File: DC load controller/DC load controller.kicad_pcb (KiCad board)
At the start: 2 copper layers, 54 x 25.4 mm, 29 parts, among them J1 Ctrl In, J2 Batt in, J3 Ctrl Out, J4 Pwr in, M1 3mm, M2 3mm, M3 3mm, Q1 BC547, Q2 BC557, U1 LM324

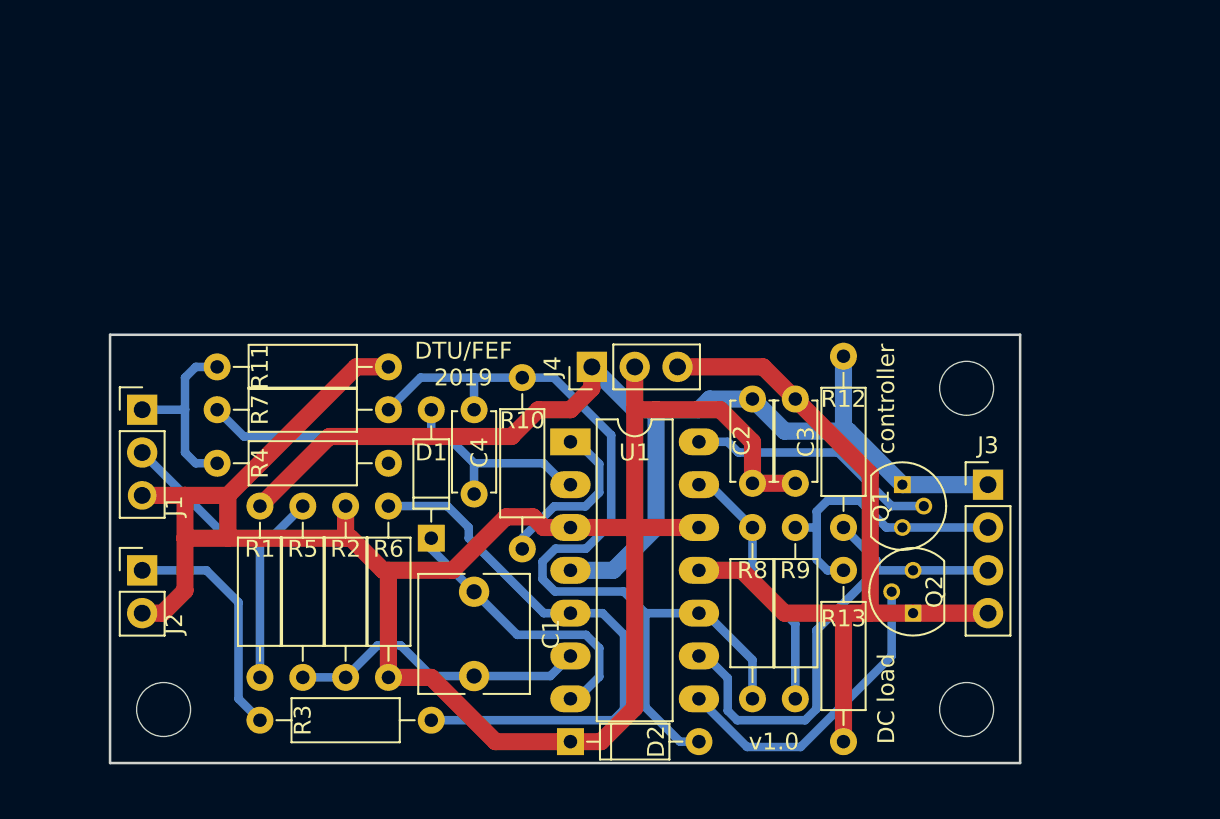
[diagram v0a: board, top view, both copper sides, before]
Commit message: Added extra output socket Layout changes
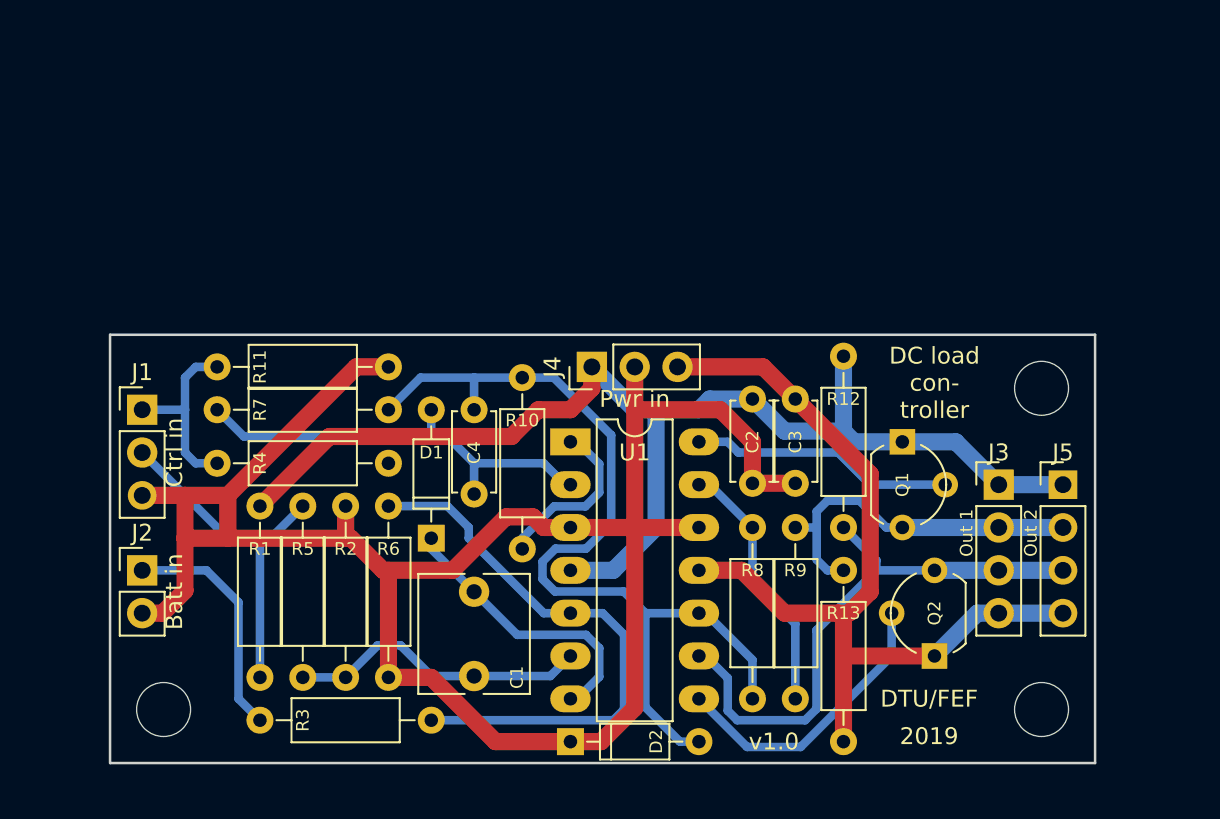
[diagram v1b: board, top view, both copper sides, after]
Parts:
- added J5: Ctrl Out 2, Pin_Headers:Pin_Header_Straight_1x04_Pitch2.54mm, F.Cu at (158.1, 72.4)
- J3: value Ctrl Out -> Ctrl Out 1
- Q1, Q2: footprint TO_SOT_Packages_THT:TO-92_Molded_Narrow -> TO_SOT_Packages_THT:TO-92_Molded_Wide
- moved M2 4.44 mm to (156.8, 85.7)
- moved M3 4.44 mm to (156.8, 66.7)
- moved Q2 2.84 mm to (150.5, 82.5)
- moved Q1 2.54 mm to (148.6, 69.8)
- moved J3 0.64 mm to (154.3, 72.4)
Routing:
- net VSS: track 48.3 -> 54.6 mm
- net Net-(J3-Pad3): track 30.0 -> 34.5 mm
- net VDD: track 68.3 -> 72.8 mm
- net Net-(J3-Pad2): track 17.1 -> 21.5 mm
- net Net-(Q2-Pad2): track 19.1 -> 17.8 mm
- net Net-(Q1-Pad2): track 15.4 -> 16.2 mm
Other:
- board size 54 x 25.4 mm -> 58.4 x 25.4 mm
- board text added: "Batt in"
- board text added: "Ctrl in"
- board text added: "DC load con- troller"
- board text added: "Out 1"
- board text added: "Out 2"
- board text added: "Pwr in"
- board text removed: "DC load"
- board text removed: "controller"

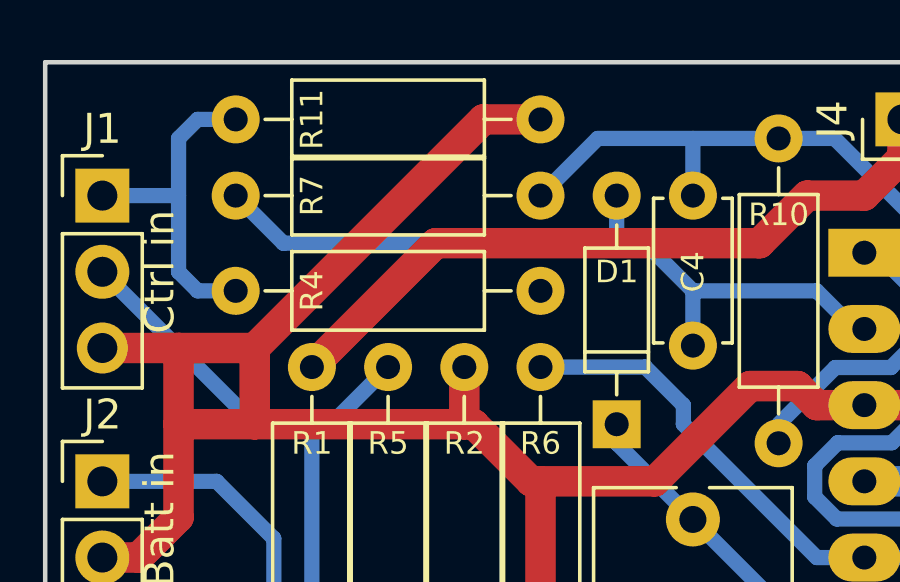
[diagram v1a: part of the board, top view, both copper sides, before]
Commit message: Fix wrong wire in schematics and pcb
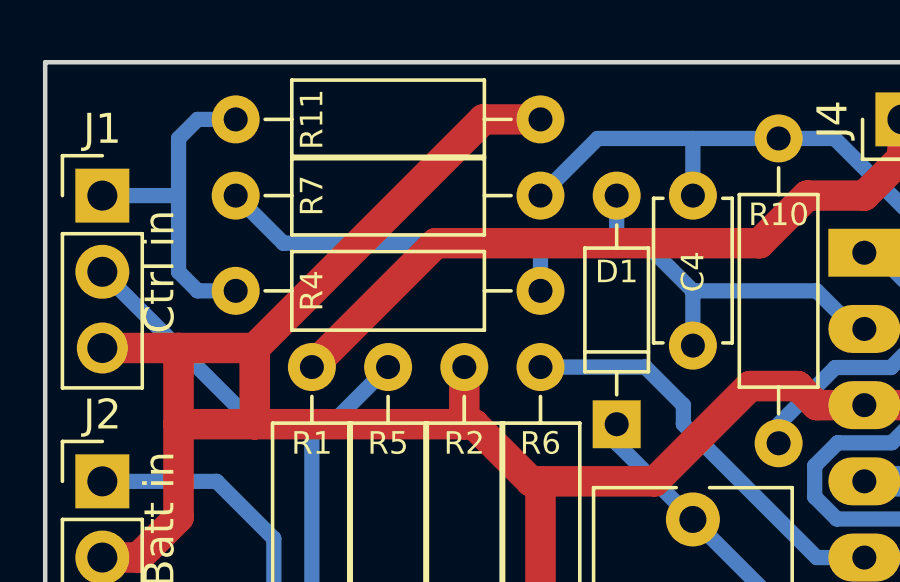
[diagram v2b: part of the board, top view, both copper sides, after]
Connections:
- R4 pad 1: Net-(R4-Pad1) -> Net-(C4-Pad1)
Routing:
- net Net-(C4-Pad1): track 26.6 -> 28.2 mm
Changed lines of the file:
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@@
 (kicad_pcb (version 4) (host pcbnew 4.0.6)
   (general
-    (links 56)
-    (no_connects 4)
-    (area 101.524999 63.424999 158.190001 88.975001)
+    (links 57)
+    (no_connects 1)
+    (area 101.524999 63.424999 160.095001 88.975001)
     (thickness 1.6)
     (drawings 13)
-    (tracks 199)
+    (tracks 201)
     (zones 0)
     (modules 30)
-    (nets 19)
+    (nets 18)
   )
   (page User 210.007 148.006)
@@
   )
   (setup
-    (last_trace_width 1.016)
+    (last_trace_width 0.508)
     (user_trace_width 0.254)
     (user_trace_width 0.508)
@@
   (net 16 "Net-(Q1-Pad2)")
   (net 17 "Net-(Q2-Pad2)")
-  (net 18 "Net-(R4-Pad1)")
   (net_class Default "This is the default net class."
     (clearance 0.2)
@@
     (add_net "Net-(R10-Pad2)")
     (add_net "Net-(R3-Pad1)")
-    (add_net "Net-(R4-Pad1)")
     (add_net "Net-(R8-Pad1)")
     (add_net VDD)
@@
     (fp_line (start 11.25 -1.6) (end -1.05 -1.6) (layer F.CrtYd) (width 0.05))
     (pad 1 thru_hole circle (at 0 0 180) (size 1.6 1.6) (drill 0.8) (layers *.Cu *.Mask)
-      (net 18 "Net-(R4-Pad1)"))
+      (net 13 "Net-(C4-Pad1)"))
     (pad 2 thru_hole oval (at 10.16 0 180) (size 1.6 1.6) (drill 0.8) (layers *.Cu *.Mask)
       (net 5 "Net-(J1-Pad1)"))
@@
   (segment (start 136.525 72.39) (end 137.16 72.39) (width 0.508) (layer B.Cu) (net 12) (status 30))
   (segment (start 137.16 72.39) (end 139.7 74.93) (width 0.508) (layer B.Cu) (net 12) (status 30))
+  (segment (start 109.5375 69.5325) (end 118.11 69.5325) (width 0.508) (layer B.Cu) (net 13))
+  (segment (start 118.11 69.5325) (end 120.65 69.5325) (width 0.508) (layer B.Cu) (net 13))
+  (segment (start 118.11 71.12) (end 118.11 69.5325) (width 0.508) (layer B.Cu) (net 13))
   (segment (start 120.65 69.5325) (end 121.6025 69.5325) (width 0.508) (layer B.Cu) (net 13))
-  (segment (start 109.5375 69.5325) (end 120.65 69.5325) (width 0.508) (layer B.Cu) (net 13))
   (segment (start 120.65 69.5325) (end 120.65 67.945) (width 0.508) (layer B.Cu) (net 13) (status 20))
   (segment (start 121.6025 69.5325) (end 123.19 71.12) (width 0.508) (layer B.Cu) (net 13))

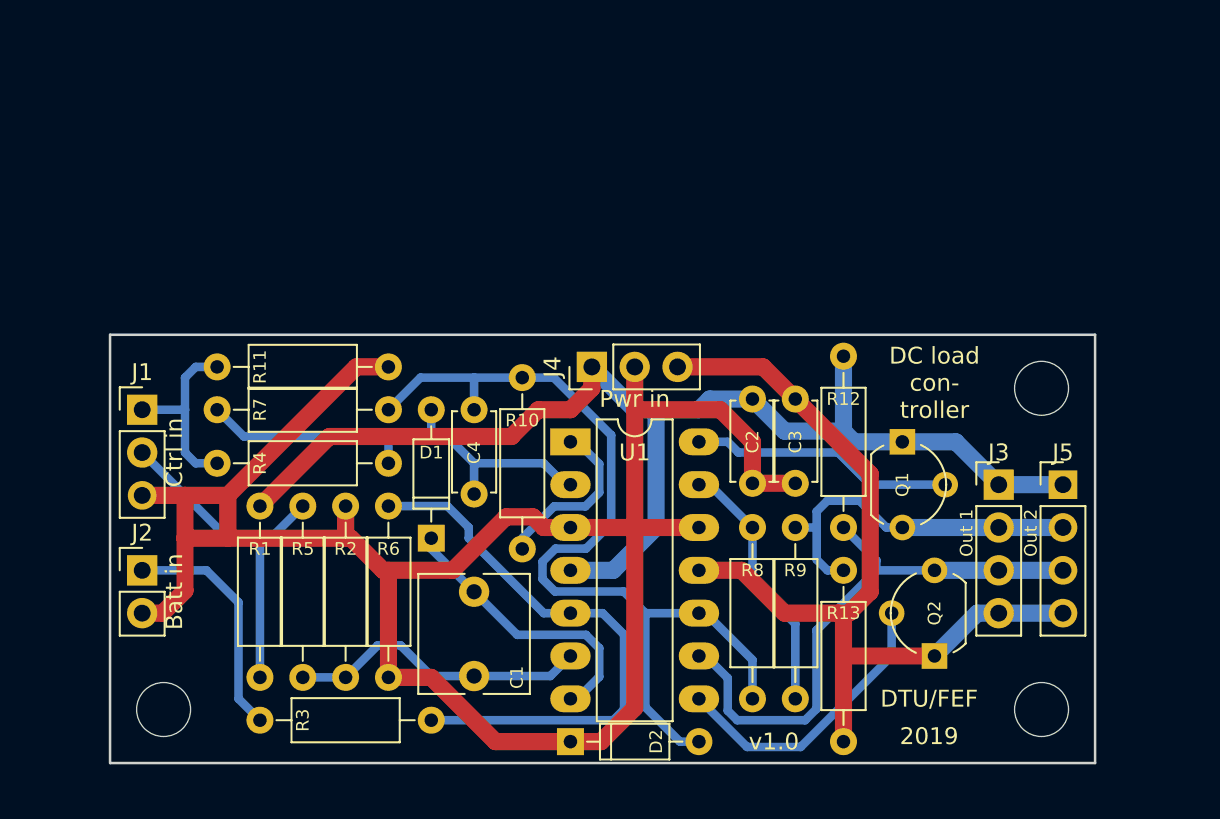
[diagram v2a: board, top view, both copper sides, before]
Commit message: Controller enhancements
Safety relay control
Input polarity check
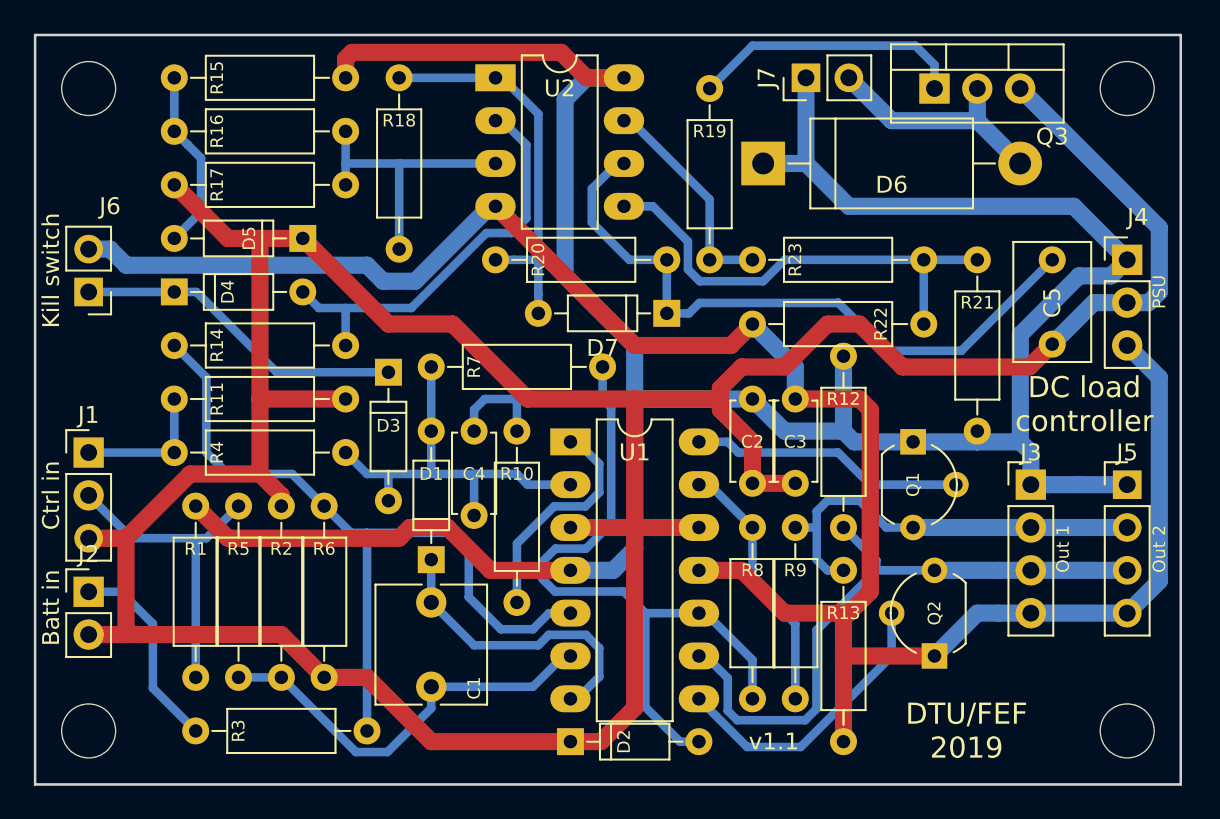
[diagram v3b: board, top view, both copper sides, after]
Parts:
- added C5: 220n, Capacitors_THT:C_Rect_L7.0mm_W4.5mm_P5.00mm, F.Cu at (157.5, 59.1)
- added D3: 1n4148, Diodes_THT:D_DO-35_SOD27_P7.62mm_Horizontal, F.Cu at (118.1, 65.7)
- added D4: 1n4148, Diodes_THT:D_DO-35_SOD27_P7.62mm_Horizontal, F.Cu at (105.4, 61.0)
- added D5: 1n4148, Diodes_THT:D_DO-35_SOD27_P7.62mm_Horizontal, F.Cu at (113.0, 57.8)
- added D6: 1n5403, Diodes_THT:D_DO-201_P15.24mm_Horizontal, F.Cu at (140.3, 53.3)
- added D7: 1n4148, Diodes_THT:D_DO-35_SOD27_P7.62mm_Horizontal, F.Cu at (134.6, 62.2)
- added J6: Killswitch, Pin_Headers:Pin_Header_Straight_1x02_Pitch2.54mm, F.Cu at (100.3, 61.0)
- added J7: Relay out, Pin_Headers:Pin_Header_Straight_1x02_Pitch2.54mm, F.Cu at (142.9, 48.3)
- added M1: 3mm, Mounting_Holes:MountingHole_3.2mm_M3, F.Cu at (100.3, 48.9)
- added Q3: IRF540N, TO_SOT_Packages_THT:TO-220-3_Vertical, F.Cu at (150.5, 48.9)
- added R14: 100k, Resistors_THT:R_Axial_DIN0207_L6.3mm_D2.5mm_P10.16mm_Horizontal, F.Cu at (115.6, 64.1)
- added R15: 10k, Resistors_THT:R_Axial_DIN0207_L6.3mm_D2.5mm_P10.16mm_Horizontal, F.Cu at (105.4, 48.3)
- added R16: 6k04, Resistors_THT:R_Axial_DIN0207_L6.3mm_D2.5mm_P10.16mm_Horizontal, F.Cu at (105.4, 51.4)
- added R17: 100, Resistors_THT:R_Axial_DIN0207_L6.3mm_D2.5mm_P10.16mm_Horizontal, F.Cu at (115.6, 54.6)
- added R18: 1M2, Resistors_THT:R_Axial_DIN0207_L6.3mm_D2.5mm_P10.16mm_Horizontal, F.Cu at (118.7, 48.3)
- added R19: 100, Resistors_THT:R_Axial_DIN0207_L6.3mm_D2.5mm_P10.16mm_Horizontal, F.Cu at (137.2, 48.9)
- added R20: 1M, Resistors_THT:R_Axial_DIN0207_L6.3mm_D2.5mm_P10.16mm_Horizontal, F.Cu at (124.5, 59.1)
- added R21: 100k, Resistors_THT:R_Axial_DIN0207_L6.3mm_D2.5mm_P10.16mm_Horizontal, F.Cu at (153.0, 69.2)
- added R22: 100k, Resistors_THT:R_Axial_DIN0207_L6.3mm_D2.5mm_P10.16mm_Horizontal, F.Cu at (149.9, 62.9)
- added R23: 1k, Resistors_THT:R_Axial_DIN0207_L6.3mm_D2.5mm_P10.16mm_Horizontal, F.Cu at (139.7, 59.1)
- added U2: LM358, Housings_DIP:DIP-8_W7.62mm_LongPads, F.Cu at (124.5, 48.3)
- Q1: value BC547 -> BC337
- Q2: value BC557 -> BC327
- R12, R13: value 10k -> 1k
- moved J4 32.4 mm to (161.9, 59.1), turned to 0 degrees
- moved M2 18.5 mm to (161.9, 48.9)
- moved R7 13.0 mm to (130.8, 65.4)
- moved M4 5.24 mm to (161.9, 87.0)
- moved M3 4.62 mm to (100.3, 87.0)
- moved J1 4.07 mm to (100.3, 70.5)
- moved R3 3.86 mm to (116.8, 87.0)
- moved J5 3.81 mm to (161.9, 72.4)
- moved R2 3.81 mm to (109.2, 73.7)
- moved R6 3.81 mm to (114.3, 73.7)
- moved R1 3.81 mm to (106.7, 73.7)
- moved R5 3.81 mm to (111.8, 83.8)
- moved J2 3.42 mm to (100.3, 78.7)
- moved R10 3.19 mm to (125.7, 69.2)
- moved R11 3.18 mm to (105.4, 67.3)
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- renumbered M3 to M2, M1 to M3, M2 to M4
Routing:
- net VDD: track 72.8 -> 160.6 mm
- net GND: track 121.0 -> 193.6 mm
- net VSS: track 54.6 -> 121.8 mm
- net Net-(C5-Pad1): track 0.00 -> 39.6 mm
- net Net-(R21-Pad2): track 0.00 -> 28.1 mm
- net Net-(D4-Pad2): track 0.00 -> 24.9 mm
- net Net-(D7-Pad2): track 0.00 -> 23.5 mm
- net Net-(D3-Pad1): track 0.00 -> 19.8 mm
- net Net-(R16-Pad2): track 0.00 -> 17.1 mm
- net Net-(Q3-Pad1): track 0.00 -> 16.3 mm
- net Net-(D6-Pad2): track 0.00 -> 14.2 mm
- net Net-(R19-Pad2): track 0.00 -> 13.1 mm
- net Net-(R14-Pad2): track 34.5 -> 47.3 mm
- net Net-(D5-Pad2): track 0.00 -> 10.8 mm
- net Net-(C1-Pad2): track 18.0 -> 24.7 mm
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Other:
- board size 58.4 x 25.4 mm -> 67.9 x 44.5 mm
- board text added: "DC load controller"
- board text added: "DTU/FEF 2019"
- board text added: "Kill switch"
- board text added: "PSU"
- board text added: "v1.1"
- board text removed: "2019"
- board text removed: "DC load con- troller"
- board text removed: "DTU/FEF"
- board text removed: "Pwr in"
- board text removed: "v1.0"

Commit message: Updated kicad version
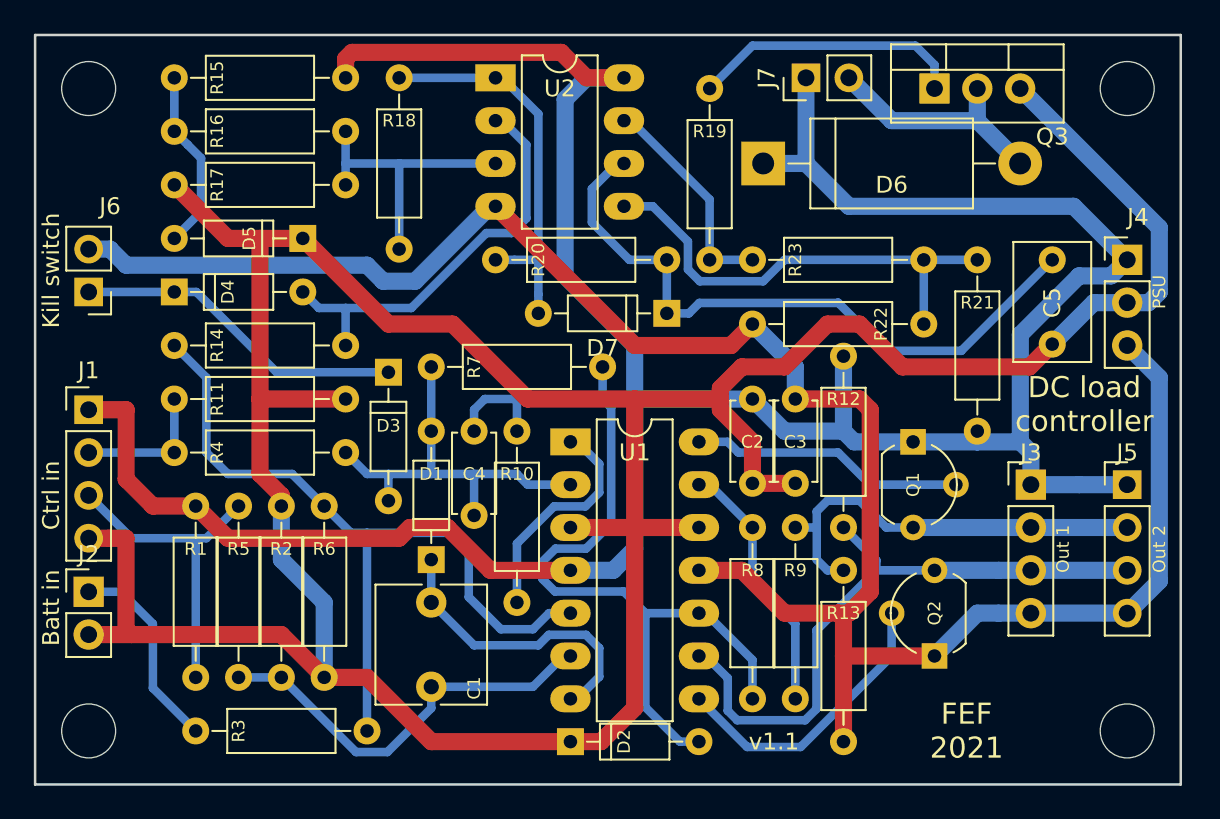
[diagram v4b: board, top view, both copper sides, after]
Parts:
- J1: footprint Pin_Headers:Pin_Header_Straight_1x03_Pitch2.54mm -> Connector_PinHeader_2.54mm:PinHeader_1x04_P2.54mm_Vertical
- moved J1 2.54 mm to (100.3, 67.9)
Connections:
- J1 pad 1: Net-(J1-Pad1) -> VDD
- J1 pad 3: GND -> Net-(J1-Pad3)
- R1 pad 2: Net-(J1-Pad2) -> Net-(J1-Pad3)
- R11 pad 1: Net-(J1-Pad1) -> Net-(J1-Pad2)
- R2 pad 1: Net-(J1-Pad2) -> Net-(J1-Pad3)
- R4 pad 2: Net-(J1-Pad1) -> Net-(J1-Pad2)
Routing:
- net Net-(J1-Pad3): track 0.00 -> 19.0 mm
- net VDD: track 160.6 -> 171.7 mm
- net Net-(J1-Pad2): track 19.0 -> 8.25 mm
- net Net-(J1-Pad1): track 8.25 -> 0.00 mm
- net GND: track 193.6 -> 195.3 mm
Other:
- board text added: "FEF 2021"
- board text removed: "DTU/FEF 2019"
